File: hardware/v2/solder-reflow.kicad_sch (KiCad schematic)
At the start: 86 parts, among them J1 I2C, J13 RTD_PT100, J14 SSROUT2, J15 LCD_CONN, J2 I2S, J3 RTD_PT100, J4 220V, J5 HEATER, J6 InputButton, J9 12VIN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

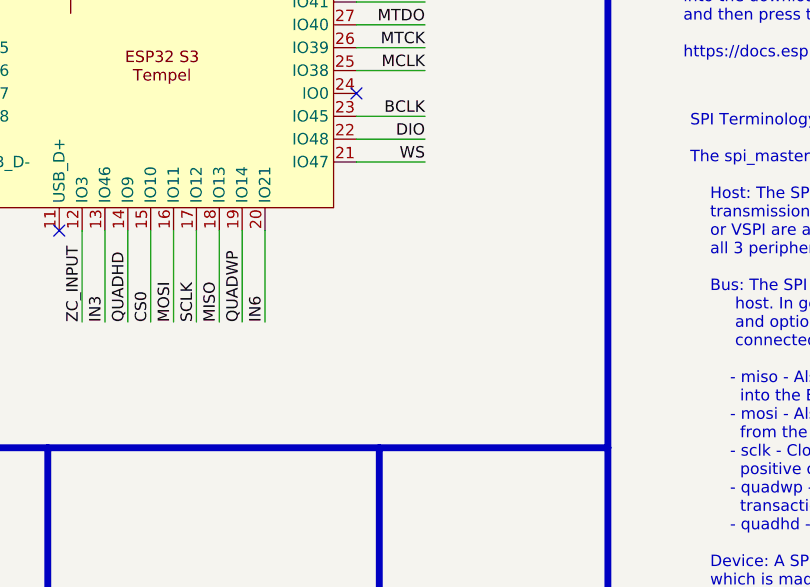
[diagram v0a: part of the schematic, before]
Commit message: feat: add led indicator
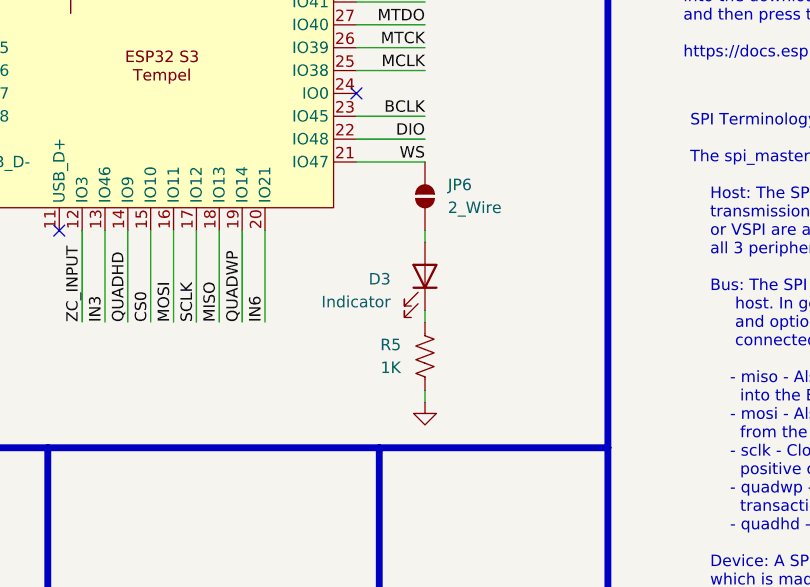
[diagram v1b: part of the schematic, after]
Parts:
- added D3: Indicator, LED_SMD:LED_1206_3216Metric_Pad1.42x1.75mm_HandSolder, symbol Device:LED
- added JP6: 2_Wire, Jumper:SolderJumper-2_P1.3mm_Open_TrianglePad1.0x1.5mm, symbol Jumper:SolderJumper_2_Open
- added R5: 1K, Resistor_SMD:R_0805_2012Metric_Pad1.20x1.40mm_HandSolder, symbol Device:R_US
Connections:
- net GND: now also R5.1
- net WS: now also JP6.2 (B)
- new net: D3.2 (A), JP6.1 (A)
- new net: D3.1 (K), R5.2
